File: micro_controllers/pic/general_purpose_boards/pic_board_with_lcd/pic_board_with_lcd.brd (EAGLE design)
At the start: 142.2 x 77.1 mm, 29 parts, among them IC1 PIC16f877a, IC2 7805TV

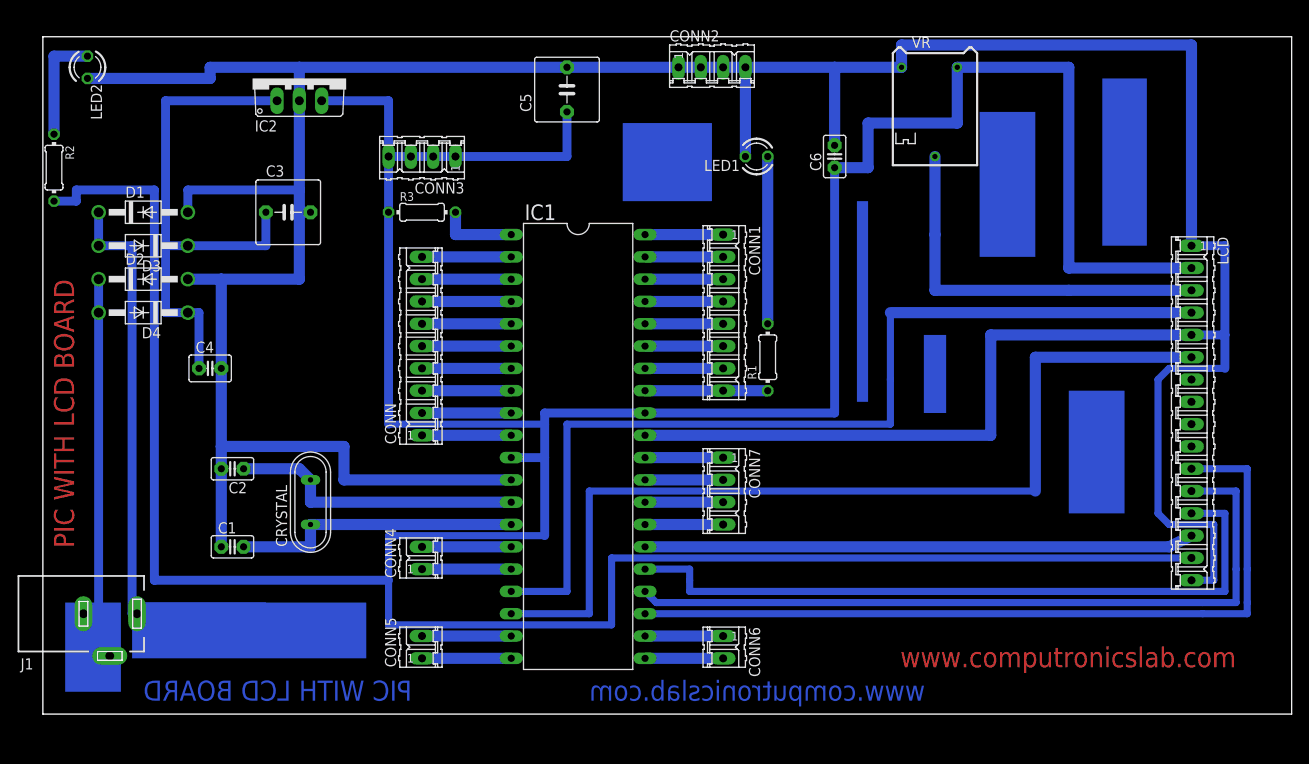
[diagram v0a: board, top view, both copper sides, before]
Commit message: 
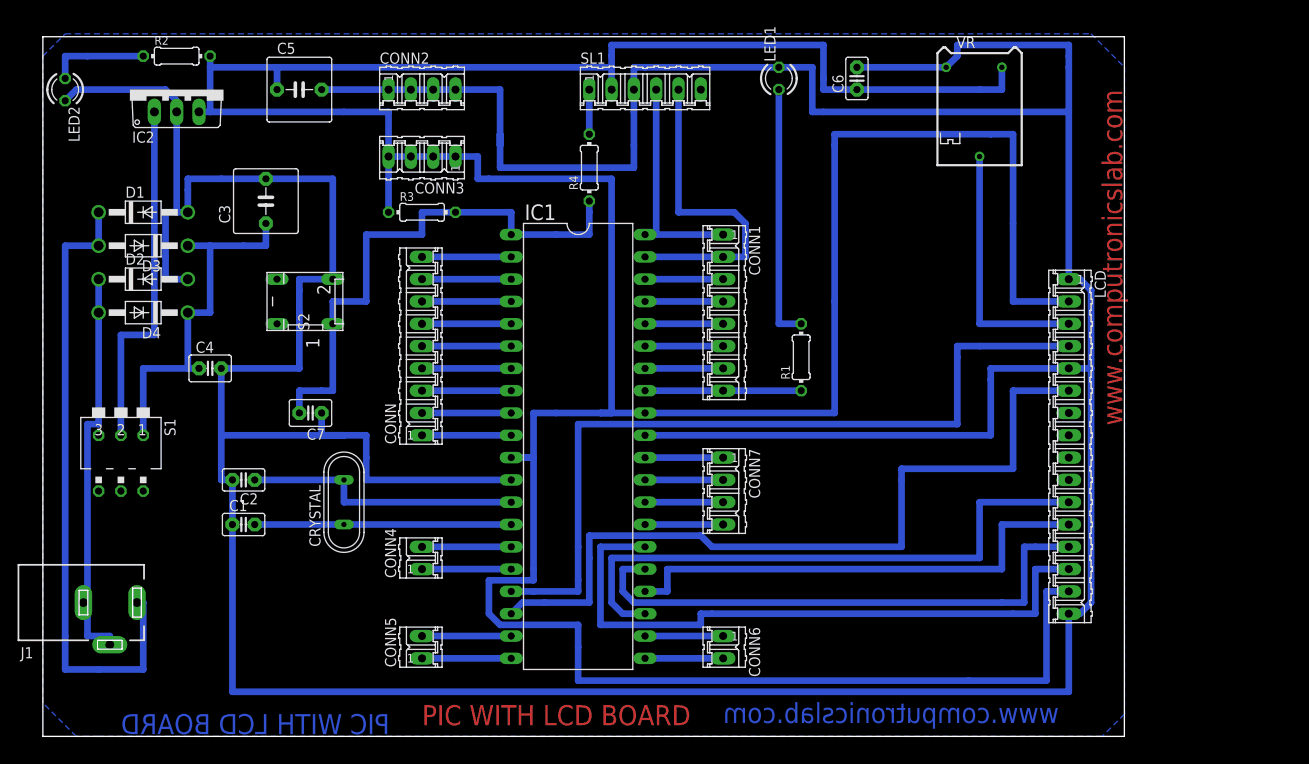
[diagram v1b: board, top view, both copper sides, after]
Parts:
- added C7: 0.1uf, capacitor-wima:C2.5-3
- added R4: 68E, rcl:0204/7
- added S1: (no value), switch-dil:DA-03
- added S2: push switch, switch-dil:DP-02
- added SL1: (no value), con-amp-quick:06P
- C3: value 1000uf -> 100uf
- C5: value 100uf -> 4.7uf
- moved CONN2 33.1 mm to (15.2, 58.4)
- moved C5 30.5 mm to (1.27, 58.4), turned to 0 degrees
- moved R2 18.9 mm to (-12.7, 62.2), turned to 0 degrees
- moved LCD 14.5 mm to (88.9, 17.8)
- moved IC2 14.0 mm to (-12.7, 58.4)
- moved C6 9.25 mm to (64.8, 59.7)
- moved LED1 9.25 mm to (55.9, 59.7), turned to 90 degrees
- moved VR 5.08 mm to (78.7, 58.4)
- moved R1 3.81 mm to (58.4, 27.9)
- moved CRYSTAL 3.81 mm to (6.35, 11.4)
- moved LED2 3.59 mm to (-25.4, 58.4)
- moved C1 2.84 mm to (-5.08, 8.89)
- moved C3 2.84 mm to (-2.54, 45.7), turned to 90 degrees
- moved C2 1.80 mm to (-5.08, 14.0)
- moved J1 1.27 mm to (-20.3, 0.00)
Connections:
- new net N$44: IC2.1, S1.2
- new net N$45: R4.2, SL1.1
- net N$19: now also SL1.4
- net N$20: now also SL1.5
- net N$30: now also S1.1; no longer IC2.1
- net N$33: now also SL1.2
- net N$35: now also C7.1, S2.2, SL1.3
- net N$39: now also C7.2, R4.1, S2.1
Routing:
- net N$35: track 426.5 -> 544.9 mm
- net N$39: track 8.89 -> 62.2 mm
- net N$44: track 0.00 -> 40.6 mm
- net N$41: track 85.6 -> 55.9 mm
- net N$20: track 8.89 -> 37.4 mm
- net N$33: track 452.1 -> 428.5 mm
- net N$38: track 91.4 -> 67.8 mm
- net N$32: track 50.1 -> 73.1 mm
- net N$30: track 62.2 -> 41.9 mm
- net N$42: track 81.3 -> 62.8 mm
- net N$19: track 8.89 -> 26.7 mm
- net N$17: track 109.2 -> 91.4 mm
- net N$46: track 106.7 -> 90.0 mm
- net N$40: track 44.5 -> 29.2 mm
- net N$43: track 62.5 -> 73.7 mm
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- added copper zone on layer 16, net N$47
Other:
- board size 142.2 x 77.1 mm -> 123.2 x 79.7 mm

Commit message: 
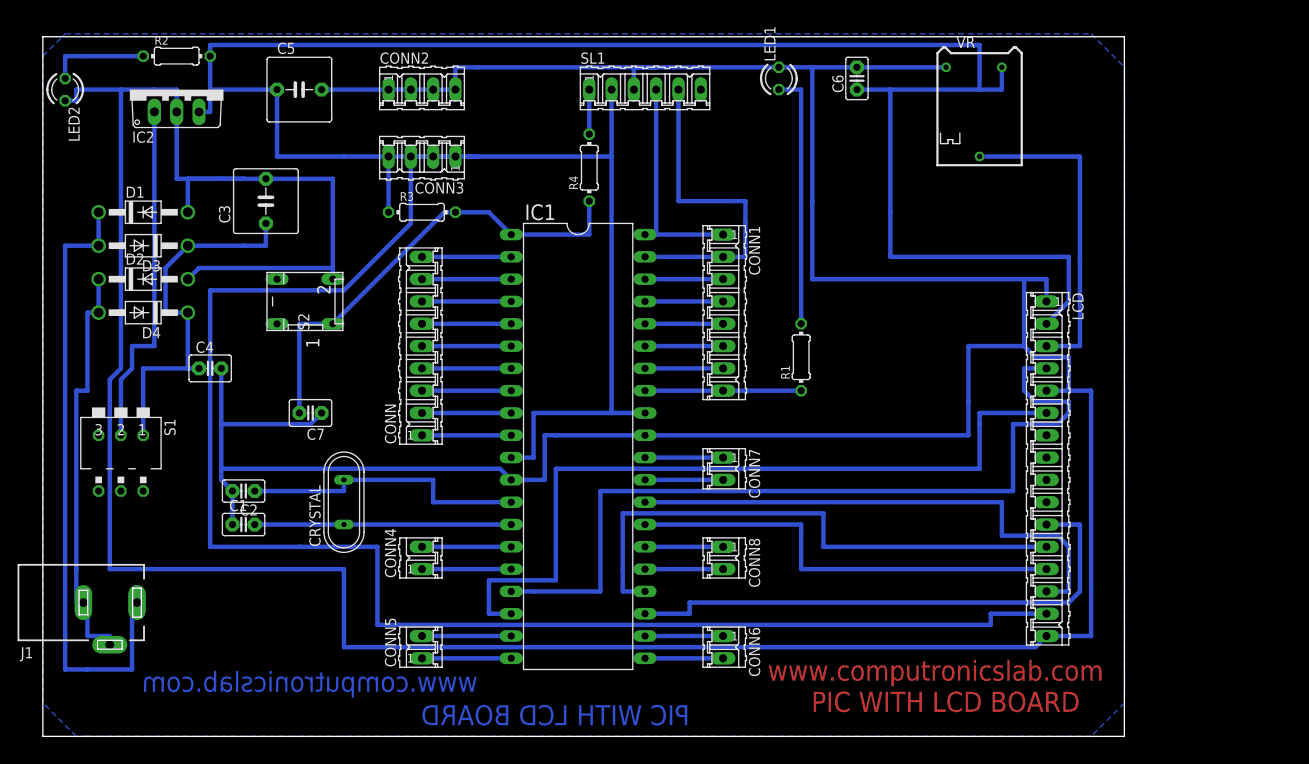
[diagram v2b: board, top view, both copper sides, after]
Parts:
- added CONN8: 2pin, con-amp-quick:02P
- CONN7: value 4 pin -> 2pin; device con-amp-quick:04P -> con-amp-quick:02P
- moved LCD 3.59 mm to (86.4, 15.2)
- moved CONN7 2.54 mm to (49.5, 15.2)
- moved C2 1.27 mm to (-5.08, 12.7)
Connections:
- removed net N$37: CONN7.4, IC1.27
- new net N$48: CONN8.1, IC1.26
- net N$36: now also CONN8.2, IC1.25; no longer CONN7.3, IC1.28
- net N$42: now also IC1.27; no longer IC1.25
- net N$43: now also IC1.28; no longer IC1.26
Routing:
- net N$33: track 428.5 -> 461.4 mm
- net N$35: track 544.9 -> 576.5 mm
- net N$43: track 73.7 -> 60.2 mm
- net N$42: track 62.8 -> 50.8 mm
- net N$39: track 62.2 -> 53.3 mm
- net N$48: track 0.00 -> 8.89 mm
- net N$37: track 8.89 -> 0.00 mm
- net N$41: track 55.9 -> 63.5 mm
- net N$40: track 29.2 -> 36.8 mm
- net N$38: track 67.8 -> 62.8 mm
- net N$17: track 91.4 -> 95.0 mm
- net N$31: track 46.4 -> 48.9 mm
- net N$32: track 73.1 -> 71.7 mm
- net N$1: track 31.8 -> 33.0 mm
- net N$46: track 90.0 -> 88.9 mm
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- added copper zone on layer 16, net N$37
- removed copper zone on layer 16, net N$47
